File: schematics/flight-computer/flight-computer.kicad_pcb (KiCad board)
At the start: 4 copper layers, 80 x 80 mm, 114 parts, among them J101 BATT, J102 CHG, J103 Expansion Slot, J104 SWD, J105 BLACKBOX, J106 USB C, J107 GPS, J108 TELEM, J301 BMI-S-201, Q401 Si9933CDY, Q402 BSS138, U101 MAX14787E, U102 STM32F405RGT6, U201 NVT2006BQ, U202 PCA9306, U203 ICM-20789, U204 MS5611-01BA, U301 Si4463, U302 MAX-M8Q, U401 BQ29200, U402 LTC4002-ES8, U403 MAX604, U404 MAX604, Y101 26M, Y301 LFTCXO068373

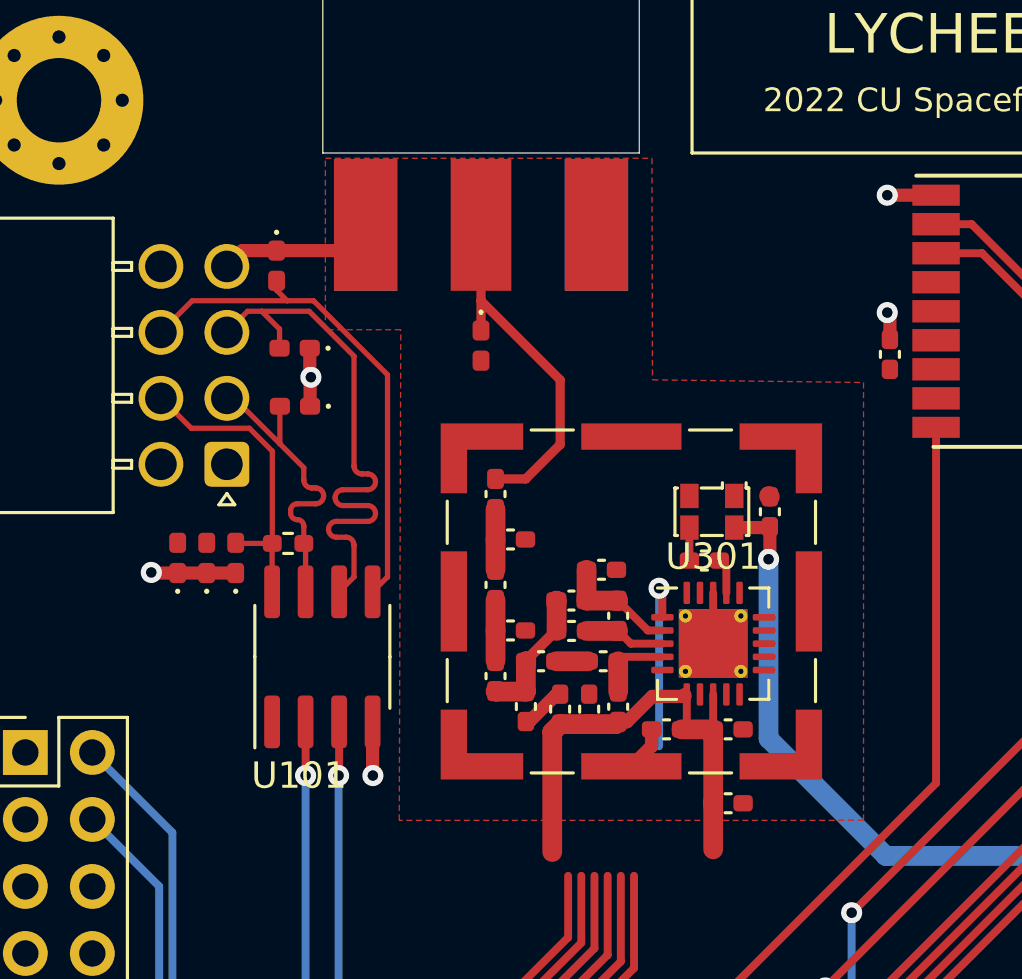
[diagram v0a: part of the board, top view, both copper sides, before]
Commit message: Fillet and stitch telemetry SMA feed
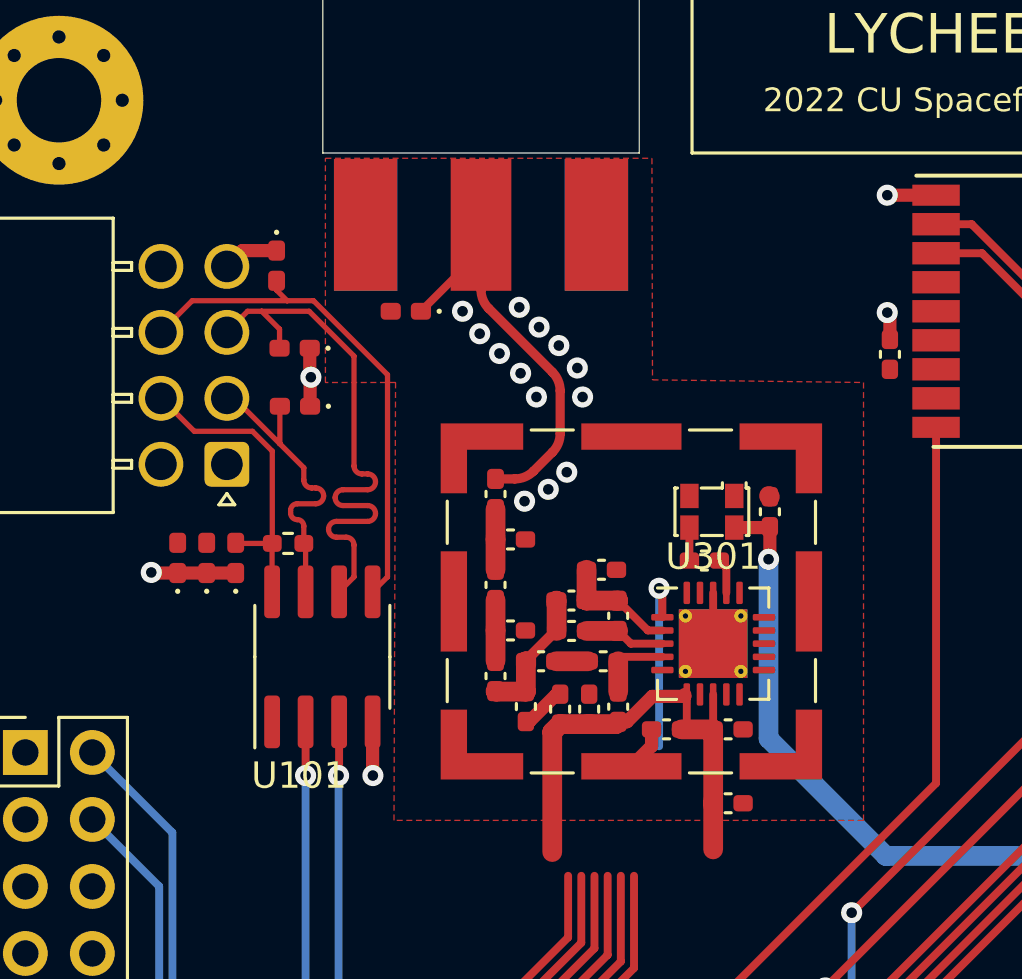
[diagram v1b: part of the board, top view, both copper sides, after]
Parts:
- moved D114 3.13 mm to (188.8, 113.1), turned to 180 degrees
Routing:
- net GND: track 103.6 -> 99.8 mm, vias 38 -> 51
- net /Radio/ANT_TLM: track 13.6 -> 16.5 mm
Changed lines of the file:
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@@
   )
   (footprint "Strix:D_0402" (layer "F.Cu")
-    (at 191.7 114.4 -90)
+    (at 188.85 113.1 180)
     (descr "Diode SMD 0402 (1005 Metric), square (rectangular) end terminal, IPC_7351 nominal, (Body size source: http://www.tortai-tech.com/upload/download/2011102023233369053.pdf), generated with kicad-footprint-generator")
     (tags "diode handsolder")
@@
     (property "Sheetname" "")
     (attr smd)
-    (fp_text reference "D114" (at 0 -1.17 90) (layer "F.Fab")
+    (fp_text reference "D114" (at 0 -1.17) (layer "F.Fab")
       (effects (font (size 1 1) (thickness 0.15)))
     )
-    (fp_text value "D_ESD" (at 0 1.17 90) (layer "F.Fab")
+    (fp_text value "D_ESD" (at 0 1.17) (layer "F.Fab")
       (effects (font (size 1 1) (thickness 0.15)))
     )
-    (fp_text user "${REFERENCE}" (at 0 0 90) (layer "F.Fab")
+    (fp_text user "${REFERENCE}" (at 0 0) (layer "F.Fab")
       (effects (font (size 0.25 0.25) (thickness 0.04)))
     )
@@
     (fp_line (start -0.3 0.25) (end -0.3 -0.25) (layer "F.Fab") (width 0.1))
     (fp_line (start -0.4 0.25) (end -0.4 -0.25) (layer "F.Fab") (width 0.1))
-    (pad "1" smd roundrect (at -0.5725 0 270) (size 0.765 0.64) (layers "F.Cu" "F.Paste" "F.Mask") (roundrect_rratio 0.25)
+    (pad "1" smd roundrect (at -0.5725 0 180) (size 0.765 0.64) (layers "F.Cu" "F.Paste" "F.Mask") (roundrect_rratio 0.25)
       (net 10 "/Radio/ANT_TLM") (pinfunction "1") (pintype "passive"))
-    (pad "2" smd roundrect (at 0.5725 0 270) (size 0.765 0.64) (layers "F.Cu" "F.Paste" "F.Mask") (roundrect_rratio 0.25)
+    (pad "2" smd roundrect (at 0.5725 0 180) (size 0.765 0.64) (layers "F.Cu" "F.Paste" "F.Mask") (roundrect_rratio 0.25)
       (net 2 "GND") (pinfunction "2") (pintype "passive"))
     (model "${KIPRJMOD}/../lib/Strix.models/D_0402.STEP"
@@
   (segment (start 238.385 137.151391) (end 239.35 137.151391) (width 0.5) (layer "F.Cu") (net 2))
   (segment (start 240.59856 122.79856) (end 240.59856 122.179304) (width 0.2) (layer "F.Cu") (net 2))
-  (segment (start 183.95 110.8) (end 186.45 110.8) (width 0.5) (layer "F.Cu") (net 2))
   (segment (start 243.875 130.4225) (end 244.675 130.4225) (width 0.5) (layer "F.Cu") (net 2))
   (segment (start 202.263499 149.8) (end 202.3175 149.8) (width 0.3) (layer "F.Cu") (net 2))
@@
   (segment (start 205.45 156.1675) (end 205.45 157.1) (width 0.3) (layer "F.Cu") (net 2))
   (segment (start 217.2 115.3) (end 218.45 115.3) (width 0.75) (layer "F.Cu") (net 2))
-  (segment (start 186.45 110.8) (end 187.325 109.925) (width 0.5) (layer "F.Cu") (net 2))
   (segment (start 209.8 159.16625) (end 211.1675 159.16625) (width 0.75) (layer "F.Cu") (net 2))
   (segment (start 203.825 155.45) (end 204.7325 155.45) (width 0.3) (layer "F.Cu") (net 2))
@@
   (via (at 188.65 160.625) (size 0.8) (drill 0.4) (layers "F.Cu" "B.Cu") (net 2))
   (via (at 205.35 164.25) (size 0.8) (drill 0.4) (layers "F.Cu" "B.Cu") (net 2))
+  (via (at 195.55 116.35) (size 0.8) (drill 0.4) (layers "F.Cu" "B.Cu") (free) (net 2))
   (via (at 207.25 158) (size 0.8) (drill 0.4) (layers "F.Cu" "B.Cu") (net 2))
   (via (at 242.21343 118.32759) (size 0.8) (drill 0.4) (layers "F.Cu" "B.Cu") (net 2))
@@
   (via (at 211.175 160.59125) (size 0.8) (drill 0.4) (layers "F.Cu" "B.Cu") (free) (net 2))
   (via (at 223.9 139.648891) (size 0.8) (drill 0.4) (layers "F.Cu" "B.Cu") (free) (net 2))
+  (via (at 194.65 114.4) (size 0.8) (drill 0.4) (layers "F.Cu" "B.Cu") (free) (net 2))
+  (via (at 195.35 115.25) (size 0.8) (drill 0.4) (layers "F.Cu" "B.Cu") (free) (net 2))
   (via (at 185.25 115.6) (size 0.8) (drill 0.4) (layers "F.Cu" "B.Cu") (free) (net 2))
   (via (at 223.9 138.648891) (size 0.8) (drill 0.4) (layers "F.Cu" "B.Cu") (free) (net 2))
+  (via (at 193.2 115.45) (size 0.8) (drill 0.4) (layers "F.Cu" "B.Cu") (free) (net 2))
   (via (at 215.4 146.348891) (size 0.8) (drill 0.4) (layers "F.Cu" "B.Cu") (free) (net 2))
   (via (at 240.344414 121.925158) (size 0.8) (drill 0.4) (layers "F.Cu" "B.Cu") (net 2))
+  (via (at 191 113.1) (size 0.8) (drill 0.4) (layers "F.Cu" "B.Cu") (free) (net 2))
+  (via (at 194.25 119.85) (size 0.8) (drill 0.4) (layers "F.Cu" "B.Cu") (free) (net 2))
+  (via (at 193.35 120.3) (size 0.8) (drill 0.4) (layers "F.Cu" "B.Cu") (free) (net 2))
   (via (at 220.9 139.648891) (size 0.8) (drill 0.4) (layers "F.Cu" "B.Cu") (free) (net 2))
+  (via (at 192.4 114.7) (size 0.8) (drill 0.4) (layers "F.Cu" "B.Cu") (free) (net 2))
+  (via (at 193.8 116.35) (size 0.8) (drill 0.4) (layers "F.Cu" "B.Cu") (free) (net 2))
+  (via (at 191.65 113.95) (size 0.8) (drill 0.4) (layers "F.Cu" "B.Cu") (free) (net 2))
   (via (at 187.6 130.7) (size 0.8) (drill 0.4) (layers "F.Cu" "B.Cu") (free) (net 2))
   (via (at 245.3 129.7975) (size 0.8) (drill 0.4) (layers "F.Cu" "B.Cu") (net 2))
@@
   (via (at 197.1505 149.8) (size 0.8) (drill 0.4) (layers "F.Cu" "B.Cu") (net 2))
   (via (at 221.9 138.648891) (size 0.8) (drill 0.4) (layers "F.Cu" "B.Cu") (free) (net 2))
+  (via (at 193.15 112.95) (size 0.8) (drill 0.4) (layers "F.Cu" "B.Cu") (free) (net 2))
   (via (at 203.25 148.7) (size 0.8) (drill 0.4) (layers "F.Cu" "B.Cu") (net 2))
   (via (at 222.9 138.648891) (size 0.8) (drill 0.4) (layers "F.Cu" "B.Cu") (free) (net 2))
   (via (at 216.4 148.348891) (size 0.8) (drill 0.4) (layers "F.Cu" "B.Cu") (free) (net 2))
+  (via (at 193.9 113.7) (size 0.8) (drill 0.4) (layers "F.Cu" "B.Cu") (free) (net 2))
   (via (at 216.4 146.348891) (size 0.8) (drill 0.4) (layers "F.Cu" "B.Cu") (free) (net 2))
   (via (at 215.4 147.348891) (size 0.8) (drill 0.4) (layers "F.Cu" "B.Cu") (free) (net 2))
+  (via (at 194.95 119.2) (size 0.8) (drill 0.4) (layers "F.Cu" "B.Cu") (free) (net 2))
   (via (at 207.1 108.7) (size 0.8) (drill 0.4) (layers "F.Cu" "B.Cu") (net 2))
   (via (at 216.8 118.8) (size 0.8) (drill 0.4) (layers "F.Cu" "B.Cu") (net 2))
@@
   (segment (start 225.7 109.925) (end 225.7 113) (width 0.355542) (layer "F.Cu") (net 9))
   (segment (start 225.7 113) (end 225.7 114.6) (width 0.355542) (layer "F.Cu") (net 9))
-  (segment (start 191.7 112.7) (end 191.7 113.8275) (width 0.35) (layer "F.Cu") (net 10))
-  (segment (start 194.7 118.15) (end 194.7 115.7) (width 0.35) (layer "F.Cu") (net 10))
-  (segment (start 193.395 119.455) (end 194.7 118.15) (width 0.35) (layer "F.Cu") (net 10))
-  (segment (start 192.25 119.455) (end 193.395 119.455) (width 0.35) (layer "F.Cu") (net 10))
-  (segment (start 194.7 115.7) (end 191.7 112.7) (width 0.35) (layer "F.Cu") (net 10))
-  (segment (start 191.7 112.7) (end 191.7 109.925) (width 0.35) (layer "F.Cu") (net 10))
+  (segment (start 191.7 110.8225) (end 191.7 109.825) (width 0.3) (layer "F.Cu") (net 10))
+  (segment (start 194.7 117.735786) (end 194.7 116.114214) (width 0.35) (layer "F.Cu") (net 10))
+  (segment (start 193.687893 119.162107) (end 194.407107 118.442893) (width 0.35) (layer "F.Cu") (net 10))
+  (segment (start 189.4225 113.1) (end 191.7 110.8225) (width 0.3) (layer "F.Cu") (net 10))
+  (segment (start 192.25 119.455) (end 192.980786 119.455) (width 0.35) (layer "F.Cu") (net 10))
+  (segment (start 194.407107 115.407107) (end 191.992893 112.992893) (width 0.35) (layer "F.Cu") (net 10))
+  (segment (start 191.7 112.285786) (end 191.7 109.925) (width 0.35) (layer "F.Cu") (net 10))
+  (arc (start 194.7 116.114214) (mid 194.62388 115.731531) (end 194.407107 115.407107) (width 0.35) (layer "F.Cu") (net 10))
+  (arc (start 194.7 117.735786) (mid 194.62388 118.118469) (end 194.407107 118.442893) (width 0.35) (layer "F.Cu") (net 10))
+  (arc (start 193.687893 119.162107) (mid 193.36347 119.37888) (end 192.980786 119.455) (width 0.35) (layer "F.Cu") (net 10))
+  (arc (start 191.992893 112.992893) (mid 191.77612 112.66847) (end 191.7 112.285786) (width 0.35) (layer "F.Cu") (net 10))
   (segment (start 240.5 137.148891) (end 240.5 137.1) (width 0.5) (layer "F.Cu") (net 11))
   (segment (start 240.5 137.1) (end 239.551391 136.151391) (width 0.5) (layer "F.Cu") (net 11))
@@
   (segment (start 217 138.45) (end 201.7 153.75) (width 0.3) (layer "B.Cu") (net 34))
   (segment (start 217 135.55) (end 217 138.45) (width 0.3) (layer "B.Cu") (net 34))
-  (segment (start 179.564994 116.385) (end 180.714505 117.534511) (width 0.2) (layer "F.Cu") (net 36))
+  (segment (start 183.787494 118.4025) (end 183.787494 121.9) (width 0.2) (layer "F.Cu") (net 36))
   (segment (start 182.4225 121.9) (end 182.4 121.8775) (width 0.2) (layer "F.Cu") (net 36))
-  (segment (start 180.714505 117.534511) (end 182.919505 117.534511) (width 0.2) (layer "F.Cu") (net 36))
-  (segment (start 183.787494 121.9) (end 183.787494 118.4025) (width 0.2) (layer "F.Cu") (net 36))
+  (segment (start 179.564994 116.385) (end 180.829994 117.65) (width 0.2) (layer "F.Cu") (net 36))
   (segment (start 183.779994 123.735) (end 183.779994 121.9075) (width 0.2) (layer "F.Cu") (net 36))
   (segment (start 183.779994 121.9075) (end 183.787494 121.9) (width 0.2) (layer "F.Cu") (net 36))
+  (segment (start 180.829994 117.65) (end 183.034994 117.65) (width 0.2) (layer "F.Cu") (net 36))
   (segment (start 183.787494 121.9) (end 182.4225 121.9) (width 0.2) (layer "F.Cu") (net 36))
-  (segment (start 182.919505 117.534511) (end 183.787494 118.4025) (width 0.2) (layer "F.Cu") (net 36))
+  (segment (start 183.034994 117.65) (end 183.787494 118.4025) (width 0.2) (layer "F.Cu") (net 36))
   (segment (start 184.481517 120.647988) (end 184.481517 120.747012) (width 0.2) (layer "F.Cu") (net 37))
   (segment (start 182.064994 116.385) (end 182.335 116.385) (width 0.2) (layer "F.Cu") (net 37))
@@
         (xy 206.2 115.8)
         (xy 206.2 132.4)
-        (xy 188.6 132.4)
-        (xy 188.658712 113.79987)
-        (xy 185.8 113.8)
+        (xy 188.400633 132.399372)
+        (xy 188.459915 115.799524)
+        (xy 185.80057 115.800282)
         (xy 185.8 107.3)
       )

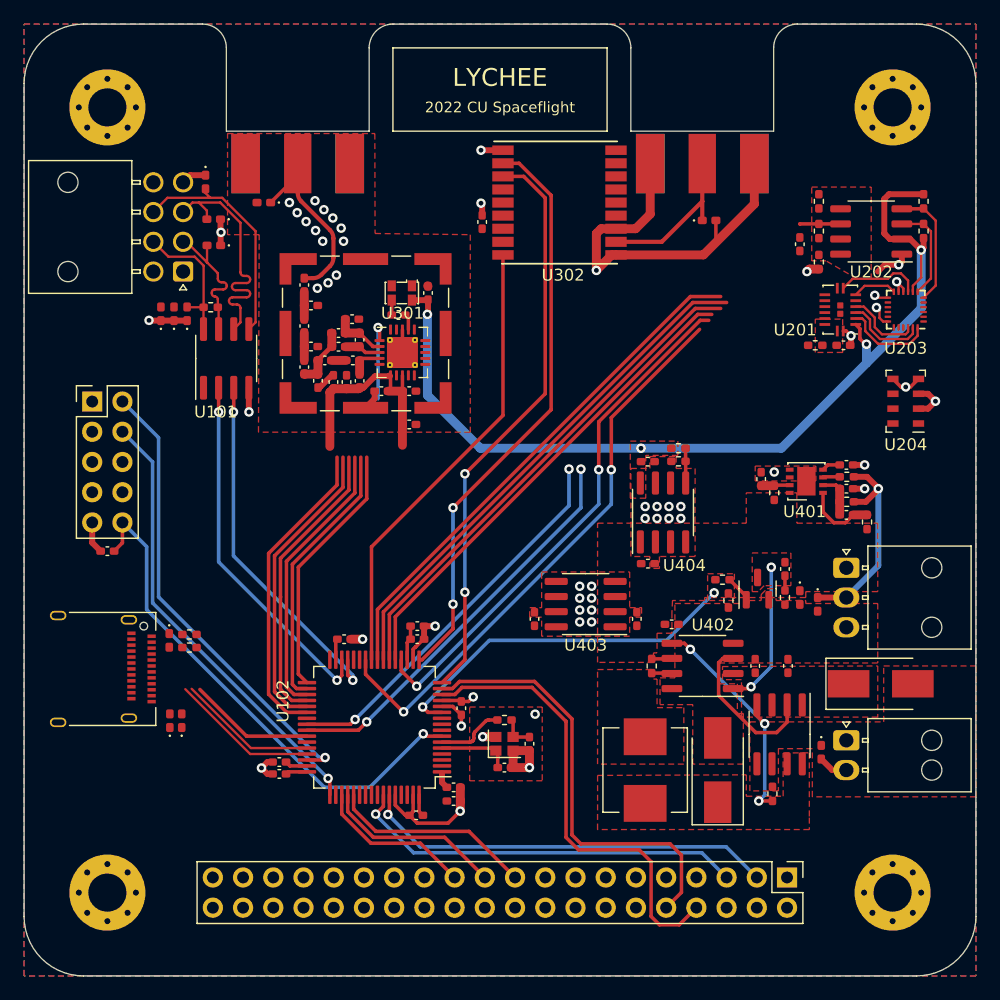
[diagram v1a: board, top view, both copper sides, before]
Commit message: Change level shifter to open drain compliant chip
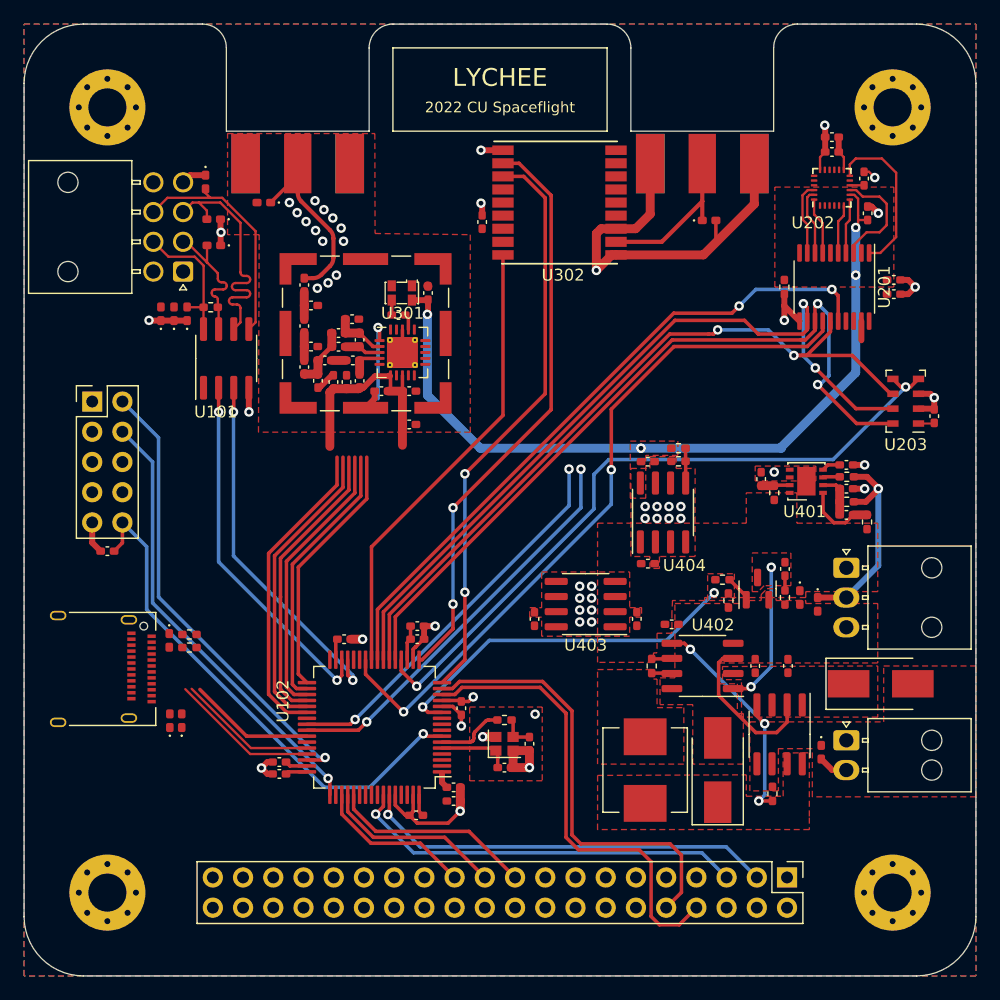
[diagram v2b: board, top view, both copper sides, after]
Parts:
- removed R201, R202, R206: 4k7, Strix:R_0402
- removed R203, R204: 200k, Strix:R_0402
- removed the U202 at (239.9, 115.5)
- added C203: 100n, Strix:C_0402, F.Cu at (241.8, 119.6)
- added C204: 2u2, Strix:C_0402, F.Cu at (236.6, 108.8)
- added C205: 100n, Strix:C_0402, F.Cu at (236.6, 107.6)
- added C206: 10n, Strix:C_0402, F.Cu at (239.6, 114.0)
- added C207: 100n, Strix:C_0402, F.Cu at (245.2, 131.1)
- C201, C202: value 100p -> 100n
- R205: value 4k7 -> 10k
- U201: value NVT2006BQ -> TXS0108EPW; footprint Strix:NVT2006BQ -> Strix:TXS0108EPW
- moved C201 14.1 mm to (239.3, 111.1), turned to -90 degrees
- moved R205 12.6 mm to (232.6, 120.2)
- moved U202 12.0 mm to (236.6, 111.8), turned to 90 degrees
- moved C202 8.95 mm to (241.8, 120.8), turned to 180 degrees
- moved U201 1.96 mm to (236.8, 120.2), turned to -90 degrees
- renumbered U203 to U202, U204 to U203
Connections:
- C202 pad 2: Net-(C202-Pad2) -> 3v3
- R205 pad 1: 1v8 -> GND
- R205 pad 2: Net-(R205-Pad2) -> 1v8
- U201 pad 1: GND -> Net-(U201-Pad1)
- U201 pad 10: /IMU_INT -> 1v8
- U201 pad 11: unconnected-(U201-Pad11) -> GND
- U201 pad 12: /IMU_~{CS} -> /SPI1_MOSI
- U201 pad 14: /SPI1_MOSI -> /IMU_~{CS}
- U201 pad 15: Net-(C201-Pad2) -> /SPI1_MISO
- U201 pad 16: Net-(C201-Pad2) -> /IMU_INT
- U201 pad 9: /SPI1_MISO -> Net-(U201-Pad9)
- U202 pad 10: GND -> Net-(C201-Pad2)
- U202 pad 12: Net-(U201-Pad7) -> Net-(U201-Pad1)
- U202 pad 22: Net-(U201-Pad5) -> Net-(U201-Pad9)
- U202 pad 23: Net-(U201-Pad4) -> Net-(U201-Pad8)
- U202 pad 24: Net-(U201-Pad3) -> Net-(U201-Pad7)
- U202 pad 6: Net-(R206-Pad2) -> Net-(U201-Pad5)
- U202 pad 7: Net-(R205-Pad2) -> Net-(U201-Pad4)
- U202 pad 9: Net-(U201-Pad8) -> Net-(U201-Pad3)
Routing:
- net /SPI1_SCLK: track 40.7 -> 66.6 mm, vias 0 -> 2
- net /SPI1_MOSI: track 43.6 -> 66.5 mm, vias 0 -> 2
- net /SPI1_MISO: track 42.3 -> 63.1 mm, vias 0 -> 2
- net 1v8: track 81.1 -> 66.3 mm
- net Net-(U201-Pad1): track 0.00 -> 13.8 mm
- net /IMU_INT: track 44.0 -> 56.4 mm, vias 0 -> 2
- net /BARO_~{CS}: track 46.8 -> 58.7 mm, vias 3 -> 2
- net /IMU_~{CS}: track 48.2 -> 59.7 mm
- net Net-(R206-Pad2): track 10.2 -> 0.00 mm
- net Net-(R205-Pad2): track 8.25 -> 0.00 mm
- net Net-(U201-Pad9): track 0.00 -> 6.17 mm
- net GND: track 99.8 -> 105.2 mm, vias 51 -> 52
- net 3v3: track 31.8 -> 35.4 mm, vias 3 -> 1
- net /I2C3_SCL: track 37.4 -> 34.0 mm
- net Net-(U201-Pad4): track 6.91 -> 4.62 mm
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- removed copper zone on F.Cu, net Net-(C202-Pad2)
- removed copper zone on F.Cu, net Net-(C302-Pad2)
